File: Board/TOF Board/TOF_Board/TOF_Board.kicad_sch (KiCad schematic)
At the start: 7 parts, among them U1 VL53L1CBV0FY-1

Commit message: updated board with library parts
Signed-off-by: EricTheGreat <joesmith01110000011101010111@gmail.com>
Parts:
- added J1: 140-506-415-000, KiCad_Cust:140-506-415-000, symbol KiCad_Cust:140-506-415-000
- added U2: AT30TS74-XM8M-T, Package_SO:MSOP-8_3x3mm_P0.65mm, symbol KiCad_Cust:AT30TS74-XM8M-T
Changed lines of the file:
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@@
   (symbol (lib_id "power:+3.3V") (at 133.35 80.01 0) (unit 1)
     (in_bom yes) (on_board yes)
-    (property "Reference" "#PWR0106" (id 0) (at 133.35 83.82 0)
+    (property "Reference" "#PWR03" (id 0) (at 133.35 83.82 0)
       (effects (font (size 1.27 1.27)) hide)
     )
@@
   (symbol (lib_id "power:+3.3V") (at 179.07 80.01 0) (unit 1)
     (in_bom yes) (on_board yes)
-    (property "Reference" "#PWR0103" (id 0) (at 179.07 83.82 0)
+    (property "Reference" "#PWR06" (id 0) (at 179.07 83.82 0)
       (effects (font (size 1.27 1.27)) hide)
     )
@@
   (symbol (lib_id "power:GND") (at 179.07 109.22 0) (unit 1)
     (in_bom yes) (on_board yes) (fields_autoplaced)
-    (property "Reference" "#PWR0101" (id 0) (at 179.07 115.57 0)
+    (property "Reference" "#PWR07" (id 0) (at 179.07 115.57 0)
       (effects (font (size 1.27 1.27)) hide)
     )
@@
   (symbol (lib_id "power:GND") (at 135.89 109.22 0) (unit 1)
     (in_bom yes) (on_board yes) (fields_autoplaced)
-    (property "Reference" "#PWR0107" (id 0) (at 135.89 115.57 0)
+    (property "Reference" "#PWR04" (id 0) (at 135.89 115.57 0)
       (effects (font (size 1.27 1.27)) hide)
     )
@@
   (symbol (lib_id "power:+3.3V") (at 127 80.01 0) (unit 1)
     (in_bom yes) (on_board yes)
-    (property "Reference" "#PWR0105" (id 0) (at 127 83.82 0)
+    (property "Reference" "#PWR02" (id 0) (at 127 83.82 0)
       (effects (font (size 1.27 1.27)) hide)
     )
@@
   (symbol (lib_id "power:+3.3V") (at 120.65 80.01 0) (unit 1)
     (in_bom yes) (on_board yes)
-    (property "Reference" "#PWR0104" (id 0) (at 120.65 83.82 0)
+    (property "Reference" "#PWR01" (id 0) (at 120.65 83.82 0)
       (effects (font (size 1.27 1.27)) hide)
     )
@@
   (symbol (lib_id "power:GND") (at 173.99 109.22 0) (unit 1)
     (in_bom yes) (on_board yes) (fields_autoplaced)
-    (property "Reference" "#PWR0102" (id 0) (at 173.99 115.57 0)
+    (property "Reference" "#PWR05" (id 0) (at 173.99 115.57 0)
       (effects (font (size 1.27 1.27)) hide)
     )
@@
     (pin "1")
   )
+  (symbol (lib_id "KiCad_Cust:AT30TS74-XM8M-T") (at 209.55 57.15 0) (unit 1)
+    (in_bom yes) (on_board yes)
+    (property "Reference" "U2" (id 0) (at 204.47 50.8 0))
+    (property "Value" "AT30TS74-XM8M-T" (id 1) (at 209.55 63.5 0))
+    (property "Footprint" "Package_SO:MSOP-8_3x3mm_P0.65mm" (id 2) (at 209.55 57.15 0)
+      (effects (font (size 1.27 1.27)) hide)
+    )
+    (property "Datasheet" "https://ww1.microchip.com/downloads/en/DeviceDoc/Web_AT30TS74_0217.pdf" (id 3) (at 209.55 57.15 0)
+      (effects (font (size 1.27 1.27)) hide)
+    )
+    (pin "1")
+    (pin "2")
+    (pin "3")
+    (pin "4")
+    (pin "5")
+    (pin "6")
+    (pin "7")
+    (pin "8")
+  )
   (symbol (lib_id "Device:R_Small_US") (at 135.89 104.14 0) (unit 1)
     (in_bom yes) (on_board yes) (fields_autoplaced)
@@
     (pin "1")
     (pin "2")
+  )
+  (symbol (lib_id "KiCad_Cust:140-506-415-000") (at 148.59 54.61 0) (unit 1)
+    (in_bom yes) (on_board yes) (fields_autoplaced)
+    (property "Reference" "J1" (id 0) (at 161.29 59.69 0)
+      (effects (font (size 1.524 1.524)) (justify left))
+    )
+    (property "Value" "140-506-415-000" (id 1) (at 161.29 63.5 0)
+      (effects (font (size 1.524 1.524)) (justify left))
+    )
+    (property "Footprint" "KiCad_Cust:140-506-415-000" (id 2) (at 158.75 61.214 0)
+      (effects (font (size 1.524 1.524)) hide)
+    )
+    (property "Datasheet" "https://files.edac.net/edac/content/series/og/English/EDAC%20140%20Series%20Standard%20(non%20WP)%20W-WW-B%20English%20Ordering%20Guide.pdf" (id 3) (at 148.59 54.61 0)
+      (effects (font (size 1.524 1.524)) hide)
+    )
+    (property "Mates with" "140-506-210-011" (id 4) (at 148.59 54.61 0)
+      (effects (font (size 1.27 1.27)) hide)
+    )
+    (property "Crimp Connectors" "140-941-290" (id 5) (at 148.59 54.61 0)
+      (effects (font (size 1.27 1.27)) hide)
+    )
+    (pin "1")
+    (pin "2")
+    (pin "3")
+    (pin "4")
+    (pin "5")
+    (pin "6")
   )
   (symbol (lib_id "KiCad_Cust:VL53L1CBV0FY-1") (at 154.94 93.98 0) (unit 1)
@@
   )
   (symbol_instances
+    (path "/9421d72d-6c35-45b9-bec5-28812acbfa17"
+      (reference "#PWR01") (unit 1) (value "+3.3V") (footprint "")
+    )
+    (path "/795cd1df-7fbd-43e5-b8c7-37253d4ed335"
+      (reference "#PWR02") (unit 1) (value "+3.3V") (footprint "")
+    )
+    (path "/25c3edd1-654a-424f-b192-1d4ebd3105bd"
+      (reference "#PWR03") (unit 1) (value "+3.3V") (footprint "")
+    )
+    (path "/701e1175-d532-4c5e-b013-c61641cdf82e"
+      (reference "#PWR04") (unit 1) (value "GND") (footprint "")
+    )
+    (path "/c568bc4c-cb07-4982-a752-1be24c63ce97"
+      (reference "#PWR05") (unit 1) (value "GND") (footprint "")
+    )
+    (path "/26d34c7a-663c-44ce-bf5d-9011a0023f0c"
+      (reference "#PWR06") (unit 1) (value "+3.3V") (footprint "")
+    )
     (path "/6419661a-a939-4852-a270-933023c6552f"
-      (reference "#PWR0101") (unit 1) (value "GND") (footprint "")
-    )
-    (path "/c568bc4c-cb07-4982-a752-1be24c63ce97"
-      (reference "#PWR0102") (unit 1) (value "GND") (footprint "")
-    )
-    (path "/26d34c7a-663c-44ce-bf5d-9011a0023f0c"
-      (reference "#PWR0103") (unit 1) (value "+3.3V") (footprint "")
-    )
-    (path "/9421d72d-6c35-45b9-bec5-28812acbfa17"
-      (reference "#PWR0104") (unit 1) (value "+3.3V") (footprint "")
-    )
-    (path "/795cd1df-7fbd-43e5-b8c7-37253d4ed335"
-      (reference "#PWR0105") (unit 1) (value "+3.3V") (footprint "")
-    )
-    (path "/25c3edd1-654a-424f-b192-1d4ebd3105bd"
-      (reference "#PWR0106") (unit 1) (value "+3.3V") (footprint "")
-    )
-    (path "/701e1175-d532-4c5e-b013-c61641cdf82e"
-      (reference "#PWR0107") (unit 1) (value "GND") (footprint "")
+      (reference "#PWR07") (unit 1) (value "GND") (footprint "")
     )
     (path "/2225601c-daae-46cb-9467-08f7096b4a9f"
@@
       (reference "C2") (unit 1) (value "4.7uF") (footprint "Resistor_SMD:R_0805_2012Metric")
     )
+    (path "/fb0b1440-18be-4b5f-b469-b4cfaf66fc53"
+      (reference "J1") (unit 1) (value "140-506-415-000") (footprint "KiCad_Cust:140-506-415-000")
+    )
     (path "/30c09179-27b1-46a1-8b7f-52075e174d5d"
       (reference "R1") (unit 1) (value "2k") (footprint "Resistor_SMD:R_0805_2012Metric")
@@
       (reference "U1") (unit 1) (value "VL53L1CBV0FY-1") (footprint "KiCad_Cust:XDCR_VL53L1CBV0FY-1")
     )
-  )
+    (path "/cb7d7a60-c3f6-41de-9a14-1e4dd5641c3a"
+      (reference "U2") (unit 1) (value "AT30TS74-XM8M-T") (footprint "Package_SO:MSOP-8_3x3mm_P0.65mm")
+    )
+  )

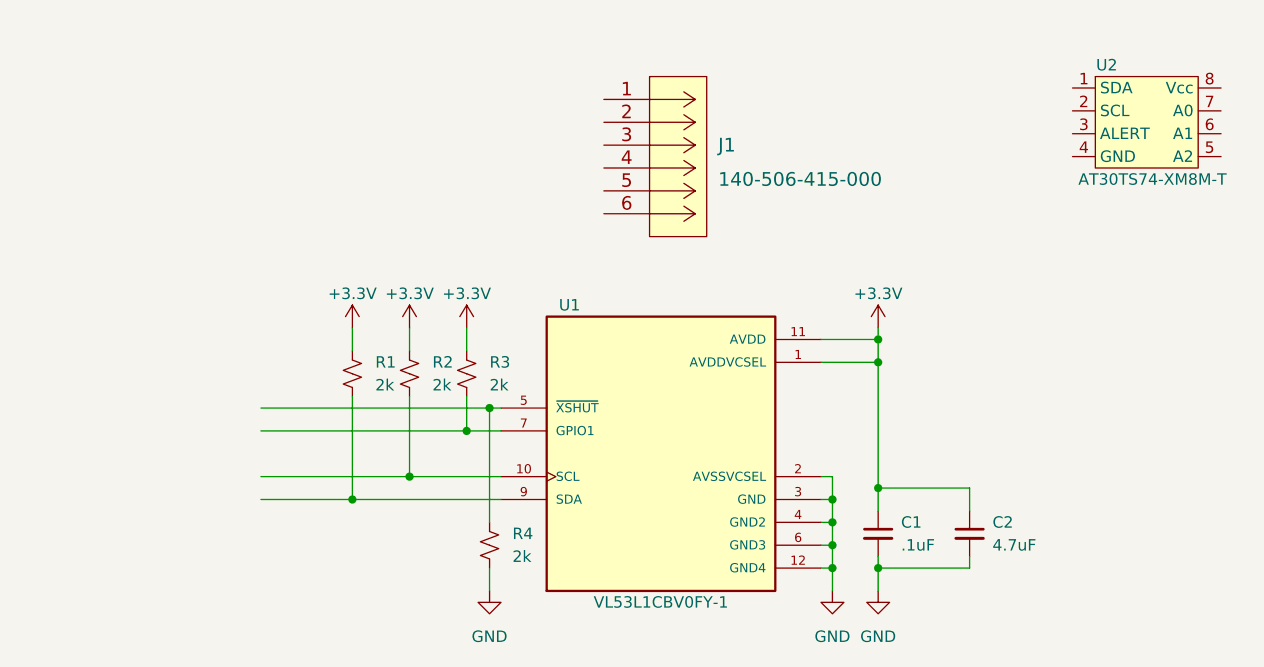
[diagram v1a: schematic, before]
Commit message: added top load connector
Signed-off-by: EricTheGreat <joesmith01110000011101010111@gmail.com>
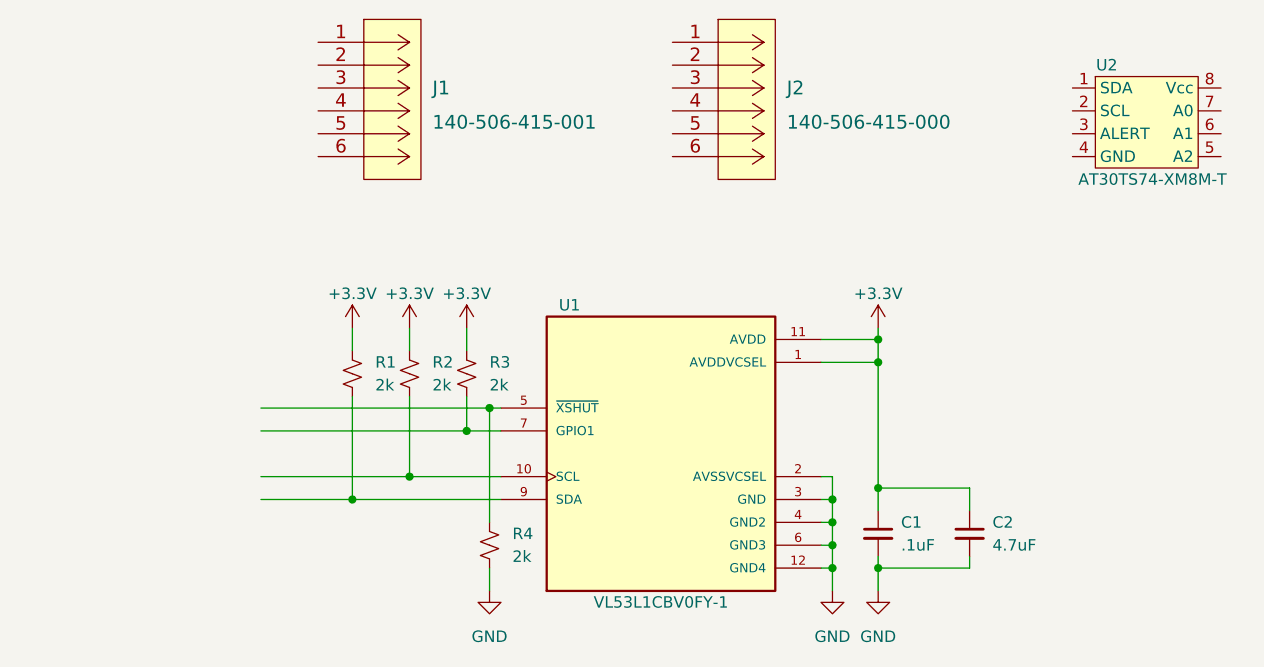
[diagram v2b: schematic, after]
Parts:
- added J1: 140-506-415-001, KiCad_Cust:140-506-415-001, symbol KiCad_Cust:140-506-415-001
- renumbered J1 to J2
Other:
- moved on the sheet: J2
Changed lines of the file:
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@@
     (pin "2")
+  )
+  (symbol (lib_id "KiCad_Cust:140-506-415-001") (at 116.84 48.26 0) (unit 1)
+    (in_bom yes) (on_board yes) (fields_autoplaced)
+    (property "Reference" "J1" (id 0) (at 129.54 53.34 0)
+      (effects (font (size 1.524 1.524)) (justify left))
+    )
+    (property "Value" "140-506-415-001" (id 1) (at 129.54 57.15 0)
+      (effects (font (size 1.524 1.524)) (justify left))
+    )
+    (property "Footprint" "KiCad_Cust:140-506-415-001" (id 2) (at 127 54.864 0)
+      (effects (font (size 1.524 1.524)) hide)
+    )
+    (property "Datasheet" "https://files.edac.net/edac/content/series/og/English/EDAC%20140%20Series%20Standard%20(non%20WP)%20W-WW-B%20English%20Ordering%20Guide.pdf" (id 3) (at 116.84 48.26 0)
+      (effects (font (size 1.524 1.524)) hide)
+    )
+    (property "Mates with" "140-506-210-011" (id 4) (at 116.84 48.26 0)
+      (effects (font (size 1.27 1.27)) hide)
+    )
+    (property "Crimp Connectors" "140-941-290" (id 5) (at 116.84 48.26 0)
+      (effects (font (size 1.27 1.27)) hide)
+    )
+    (pin "1")
+    (pin "2")
+    (pin "3")
+    (pin "4")
+    (pin "5")
+    (pin "6")
   )
   (symbol (lib_id "Device:R_Small_US") (at 133.35 85.09 0) (unit 1)
@@
     (pin "2")
   )
-  (symbol (lib_id "KiCad_Cust:140-506-415-000") (at 148.59 54.61 0) (unit 1)
-    (in_bom yes) (on_board yes) (fields_autoplaced)
-    (property "Reference" "J1" (id 0) (at 161.29 59.69 0)
-      (effects (font (size 1.524 1.524)) (justify left))
-    )
-    (property "Value" "140-506-415-000" (id 1) (at 161.29 63.5 0)
-      (effects (font (size 1.524 1.524)) (justify left))
-    )
-    (property "Footprint" "KiCad_Cust:140-506-415-000" (id 2) (at 158.75 61.214 0)
-      (effects (font (size 1.524 1.524)) hide)
-    )
-    (property "Datasheet" "https://files.edac.net/edac/content/series/og/English/EDAC%20140%20Series%20Standard%20(non%20WP)%20W-WW-B%20English%20Ordering%20Guide.pdf" (id 3) (at 148.59 54.61 0)
-      (effects (font (size 1.524 1.524)) hide)
-    )
-    (property "Mates with" "140-506-210-011" (id 4) (at 148.59 54.61 0)
-      (effects (font (size 1.27 1.27)) hide)
-    )
-    (property "Crimp Connectors" "140-941-290" (id 5) (at 148.59 54.61 0)
+  (symbol (lib_id "KiCad_Cust:140-506-415-000") (at 156.21 48.26 0) (unit 1)
+    (in_bom yes) (on_board yes) (fields_autoplaced)
+    (property "Reference" "J2" (id 0) (at 168.91 53.34 0)
+      (effects (font (size 1.524 1.524)) (justify left))
+    )
+    (property "Value" "140-506-415-000" (id 1) (at 168.91 57.15 0)
+      (effects (font (size 1.524 1.524)) (justify left))
+    )
+    (property "Footprint" "KiCad_Cust:140-506-415-000" (id 2) (at 166.37 54.864 0)
+      (effects (font (size 1.524 1.524)) hide)
+    )
+    (property "Datasheet" "https://files.edac.net/edac/content/series/og/English/EDAC%20140%20Series%20Standard%20(non%20WP)%20W-WW-B%20English%20Ordering%20Guide.pdf" (id 3) (at 156.21 48.26 0)
+      (effects (font (size 1.524 1.524)) hide)
+    )
+    (property "Mates with" "140-506-210-011" (id 4) (at 156.21 48.26 0)
+      (effects (font (size 1.27 1.27)) hide)
+    )
+    (property "Crimp Connectors" "140-941-290" (id 5) (at 156.21 48.26 0)
       (effects (font (size 1.27 1.27)) hide)
     )
@@
       (reference "C2") (unit 1) (value "4.7uF") (footprint "Resistor_SMD:R_0805_2012Metric")
     )
+    (path "/456c5e47-d71e-4708-b061-1e61634d8648"
+      (reference "J1") (unit 1) (value "140-506-415-001") (footprint "KiCad_Cust:140-506-415-001")
+    )
     (path "/fb0b1440-18be-4b5f-b469-b4cfaf66fc53"
-      (reference "J1") (unit 1) (value "140-506-415-000") (footprint "KiCad_Cust:140-506-415-000")
+      (reference "J2") (unit 1) (value "140-506-415-000") (footprint "KiCad_Cust:140-506-415-000")
     )
     (path "/30c09179-27b1-46a1-8b7f-52075e174d5d"

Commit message: TOF board done (for now)
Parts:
- removed J2: 140-506-415-000, KiCad_Cust:140-506-415-000, symbol KiCad_Cust:140-506-415-000
- removed R1, R2, R3: 2k, Resistor_SMD:R_0805_2012Metric, symbol Device:R_Small_US
- removed U2: AT30TS74-XM8M-T, Package_SO:MSOP-8_3x3mm_P0.65mm, symbol KiCad_Cust:AT30TS74-XM8M-T
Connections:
- net +3V3: now also J1.6, R4.1
- net GND: now also J1.1, J1.2; no longer R4.2
- net at U1.9 (SDA): now also J1.4
- net at J1.3: now also U1.10 (SCL)
- net at J1.5: now also U1.7 (GPIO1)
- net at U1.5 (~{XSHUT}): now also R4.2; no longer R4.1
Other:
- moved on the sheet: J1, R4
